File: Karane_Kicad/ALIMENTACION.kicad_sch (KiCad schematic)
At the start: 17 parts, among them J11 Conn_01x02_Socket, J9 Conn_01x02_Socket, SW4 SW_Push_SPDT, U24 CN3903

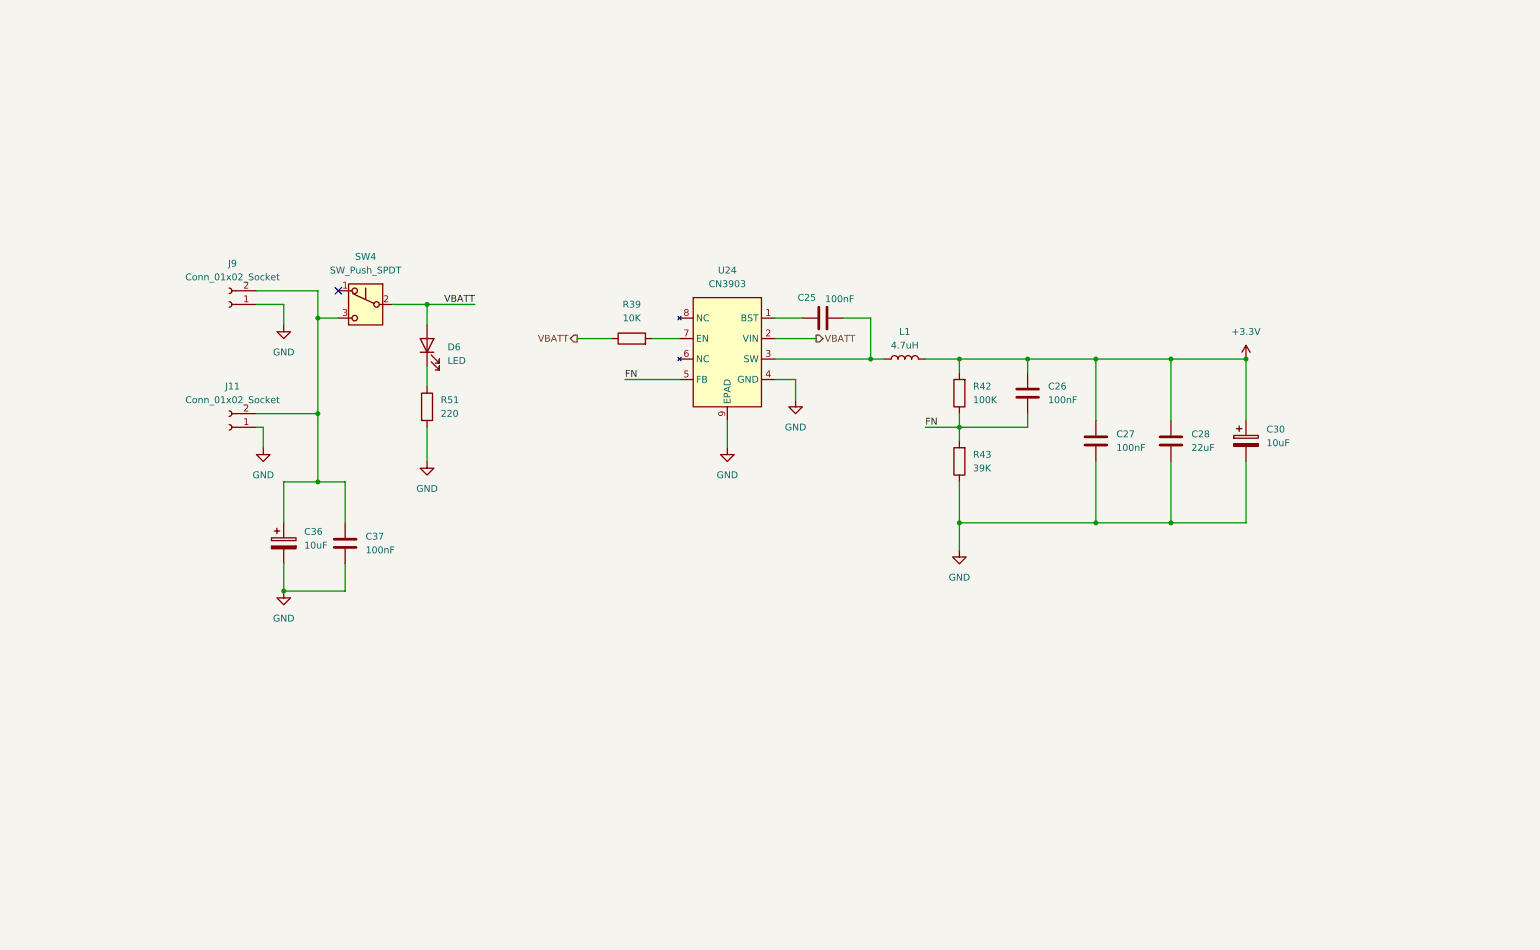
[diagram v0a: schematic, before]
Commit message: Agregado Mosfet dual
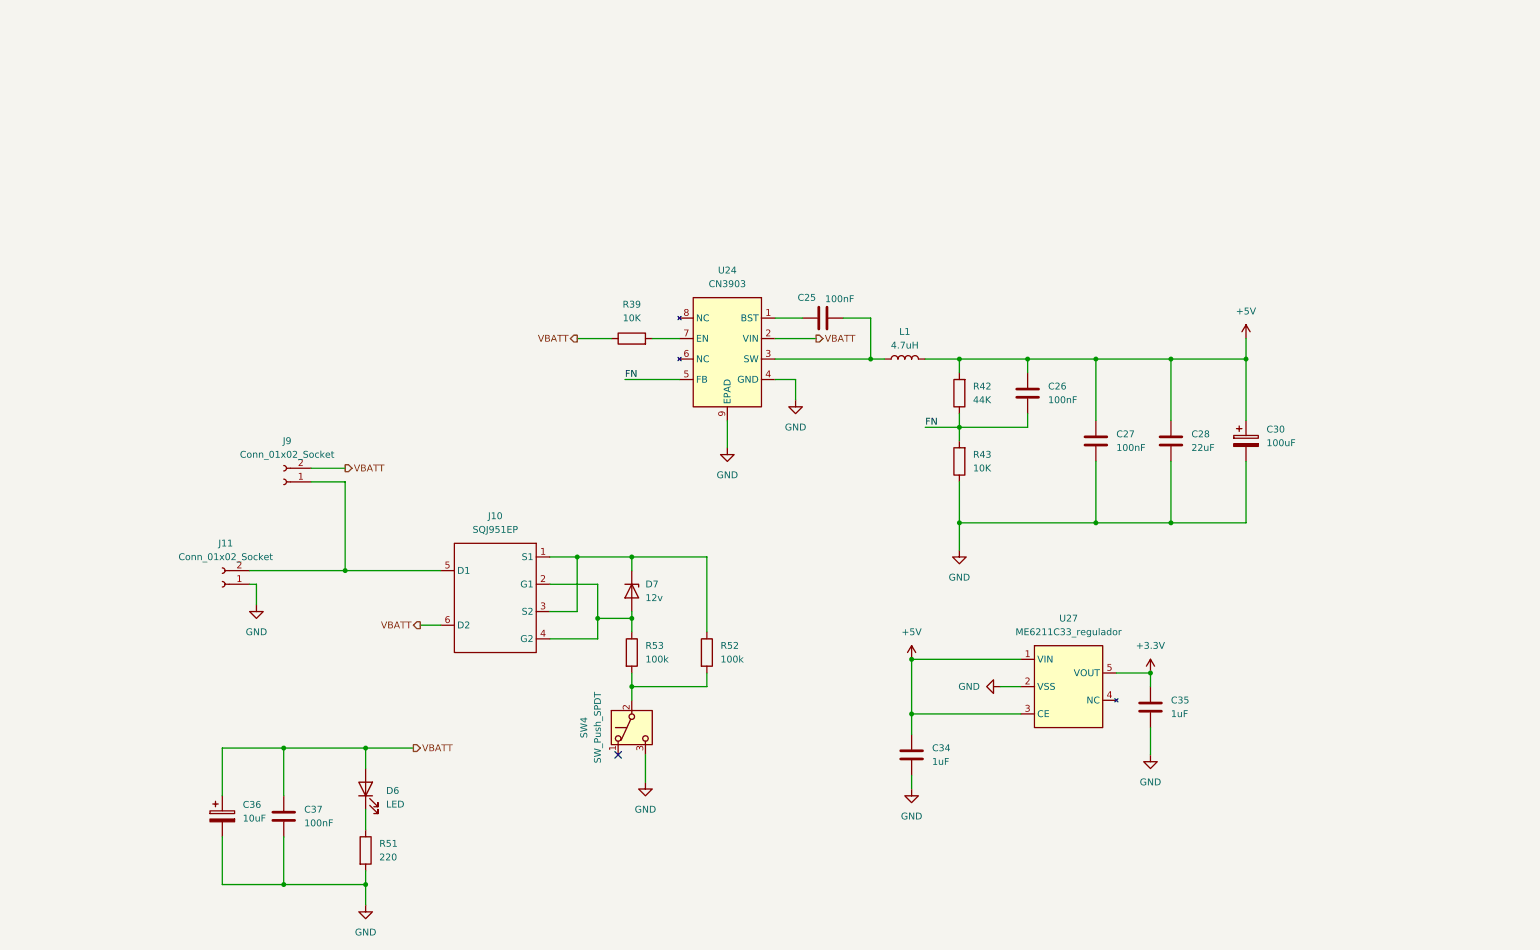
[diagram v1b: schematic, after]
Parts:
- added C34, C35: 1uF, Capacitor_SMD:C_0603_1608Metric_Pad1.08x0.95mm_HandSolder, symbol Device:C
- added D7: 12v, symbol Device:D_Zener
- added J10: SQJ951EP, Package_SO:PowerPAK_SO-8_Dual, symbol Micromouse_Library:SQJ951EP-T1_BE3
- added R52, R53: 100k, Resistor_SMD:R_0805_2012Metric_Pad1.20x1.40mm_HandSolder, symbol Device:R
- added U27: ME6211C33_regulador, Package_TO_SOT_SMD:SOT-23-5_HandSoldering, symbol Micromouse_Library:ME6211C33_regulador
- C30: value 10uF -> 100uF
- R42: value 100K -> 44K
- R43: value 39K -> 10K
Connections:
- net +3.3V: now also C35.1, U27.5 (VOUT); no longer C26.1, C27.1, C28.1, C30.1, L1.2, R42.2
- net GND: now also SW4.3 (C), C34.2, C35.2, U27.2 (VSS); no longer J9.1 (Pin_1)
- net VBATT: now also C36.1, C37.1, J9.2 (Pin_2), J10.6 (D2); no longer SW4.2 (B)
- new net: D7.1 (K), J10.1 (S1), J10.3 (S2), R52.1
- new net: D7.2 (A), J10.2 (G1), J10.4 (G2), R53.1
- new net: J10.5 (D1), J11.2 (Pin_2), J9.1 (Pin_1)
- new net: R52.2, R53.2, SW4.2 (B)
- new net +5V: C26.1, C27.1, C28.1, C30.1, C34.1, L1.2, R42.2, U27.1 (VIN), U27.3 (CE)
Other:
- moved on the sheet: C36, C37, D6, J11, J9, R51, SW4

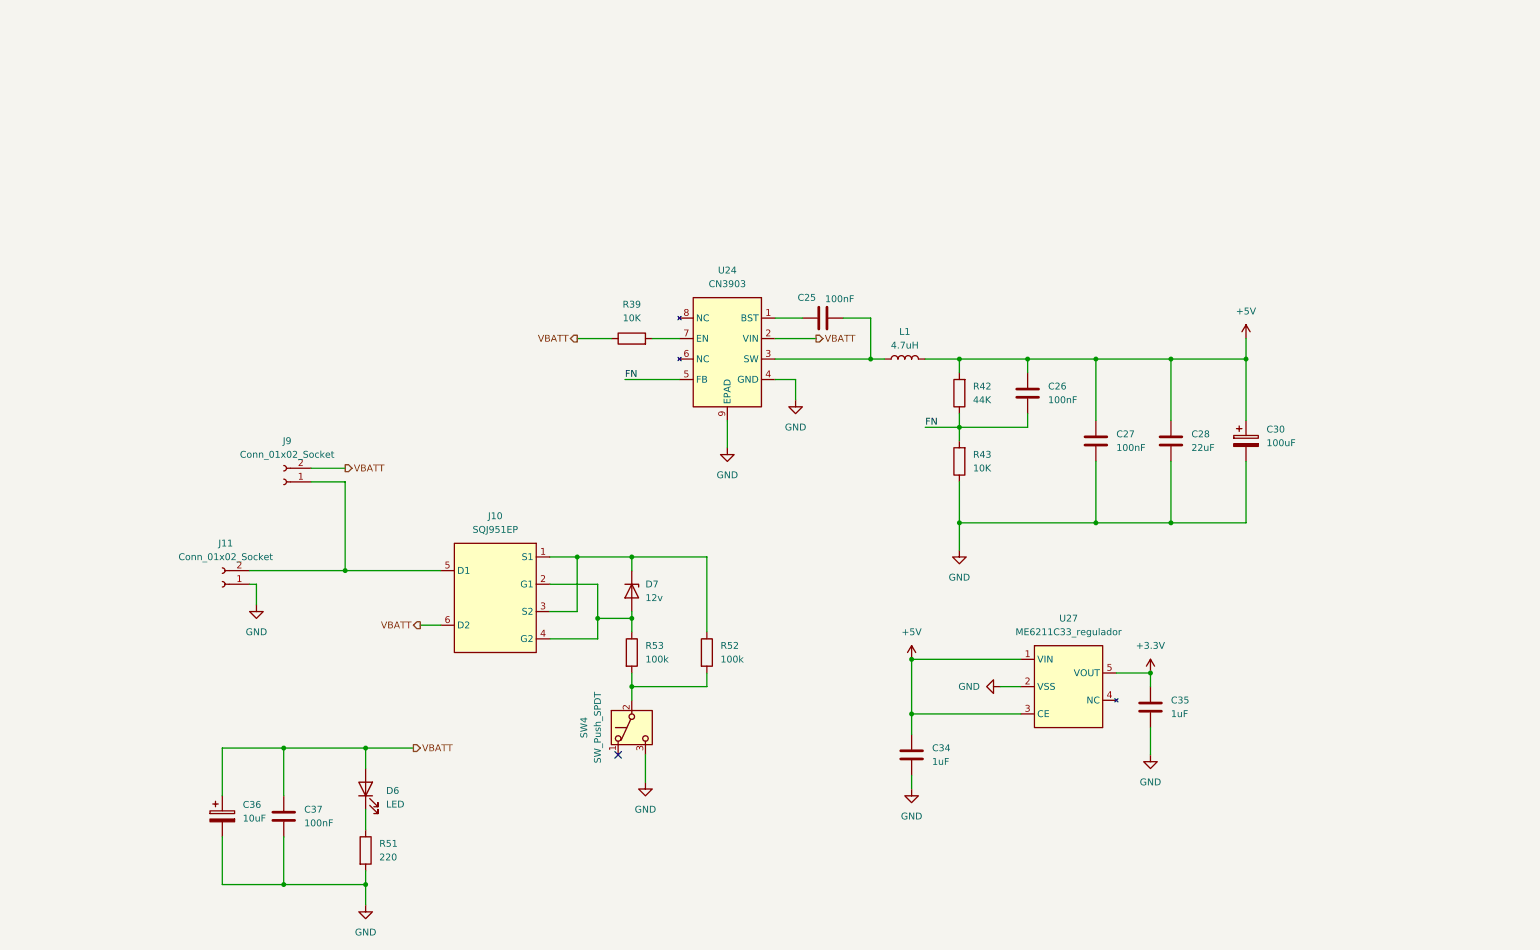
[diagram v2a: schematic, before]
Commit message: Agregado symbol de mosfet
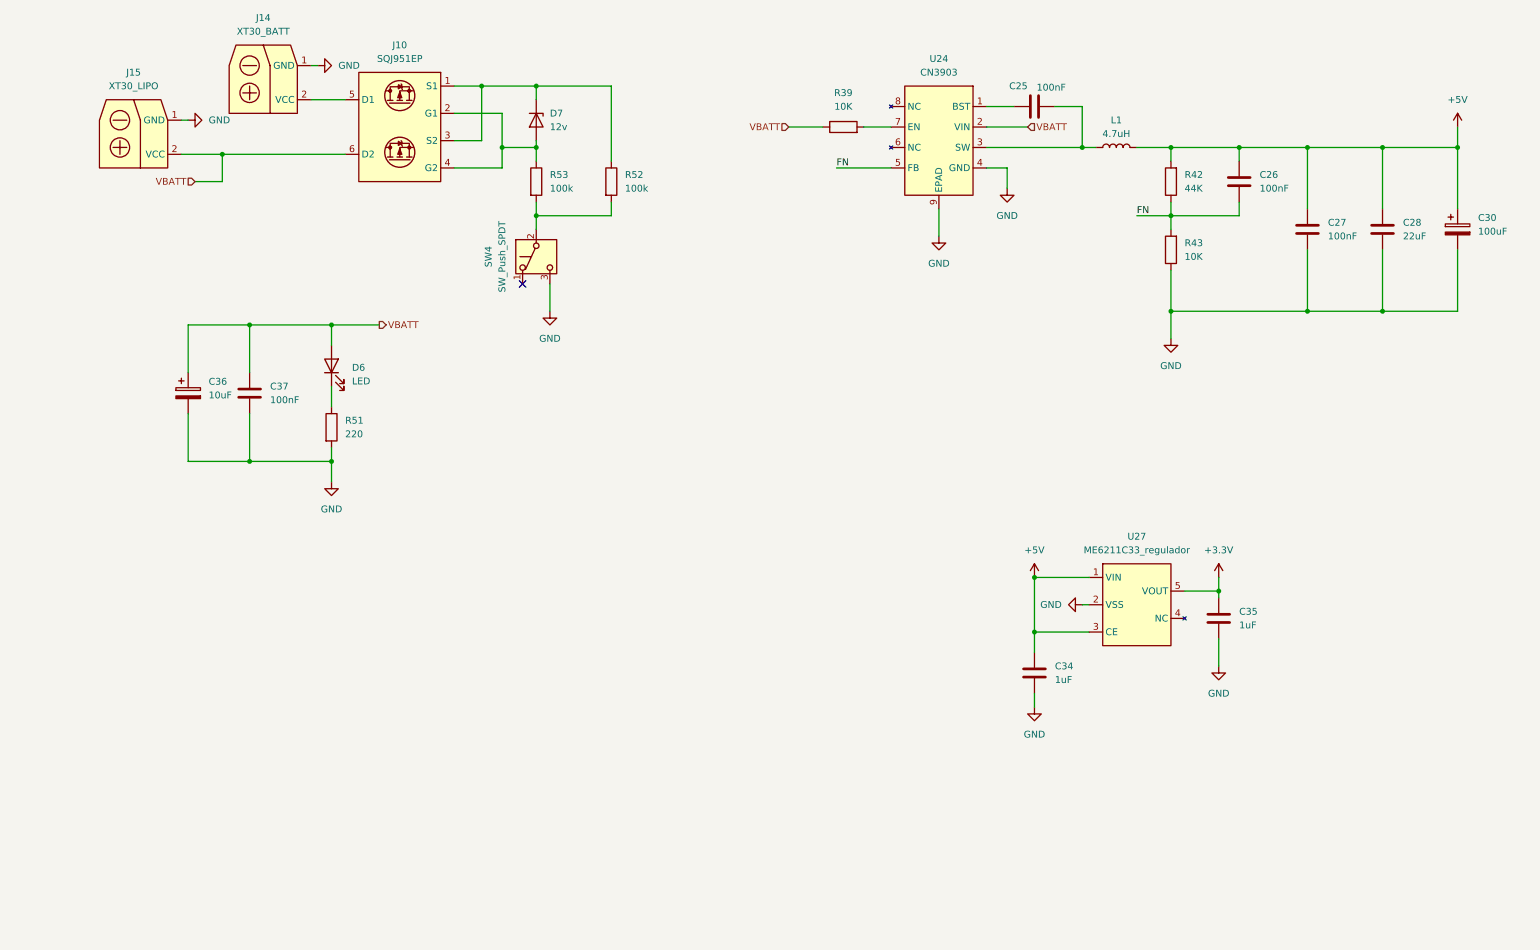
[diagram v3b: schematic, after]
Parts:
- removed J11, J9: Conn_01x02_Socket, Connector_Samtec_HPM_THT:Samtec_HPM-02-01-x-S_Straight_1x02_Pitch5.08mm, symbol Connector:Conn_01x02_Socket
- added J14: XT30_BATT, Connector_AMASS:AMASS_XT30U-F_1x02_P5.0mm_Vertical, symbol Micromouse_Library:Conector_XT30
- added J15: XT30_LIPO, Connector_AMASS:AMASS_XT30U-F_1x02_P5.0mm_Vertical, symbol Micromouse_Library:Conector_XT30
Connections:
- net GND: now also J14.1 (GND), J15.1 (GND)
- net VBATT: now also J15.2 (VCC)
- net at J10.5 (D1): now also J14.2 (VCC)
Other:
- moved on the sheet: C25, C26, C27, C28, C30, C34, C35, C36, C37, D6, D7, L1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

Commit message: Cambio de f103 a f401
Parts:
- removed D7: 12v, symbol Device:D_Zener
- removed J10: SQJ951EP, Package_SO:PowerPAK_SO-8_Dual, symbol Micromouse_Library:SQJ951EP-T1_BE3
- removed J15: XT30_LIPO, Connector_AMASS:AMASS_XT30U-F_1x02_P5.0mm_Vertical, symbol Micromouse_Library:Conector_XT30
- removed R52, R53: 100k, Resistor_SMD:R_0805_2012Metric_Pad1.20x1.40mm_HandSolder, symbol Device:R
- removed SW4: SW_Push_SPDT, Button_Switch_SMD:SW_SPDT_PCM12, symbol Switch:SW_Push_SPDT
- added D9: 12v, Diode_SMD:D_1206_3216Metric_Pad1.42x1.75mm_HandSolder, symbol Device:D_Zener
- added J11: XT30_BATT, Connector_AMASS:AMASS_XT30U-F_1x02_P5.0mm_Vertical, symbol Micromouse_Library:Conector_XT30
- added J12, J13: SQJ951EP, Package_SO:PowerPAK_SO-8_Dual, symbol Micromouse_Library:SQJ951EP-T1_BE3
- added R55, R57: 100k, Resistor_SMD:R_0805_2012Metric_Pad1.20x1.40mm_HandSolder, symbol Device:R
- added SW5: SW_Push_SPDT, Button_Switch_SMD:SW_SPDT_PCM12, symbol Switch:SW_Push_SPDT
- J14: value XT30_BATT -> XT30_LIPO
- renumbered C36 to C29, C37 to C30, C25 to C31, C34 to C32, C35 to C33, C26 to C34, C27 to C35, C28 to C36, C30 to C37, D6 to D10, R51 to R56, R39 to R58, R42 to R59, R43 to R60, U24 to U25, U27 to U26
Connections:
- net GND: now also J11.1 (GND), SW5.2 (B)
- net VBATT: now also J14.2 (VCC), J13.5 (D1), J13.6 (D2)
- new net: J11.2 (VCC), J12.5 (D1), J12.6 (D2)
- new net: D9.1 (K), J12.1 (S1), J12.3 (S2), J13.1 (S1), J13.3 (S2), R57.1
- new net: R55.2, R57.2, SW5.1 (A)
- new net: D9.2 (A), J12.2 (G1), J12.4 (G2), J13.2 (G1), J13.4 (G2), R55.1
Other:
- moved on the sheet: C29, C30, D10, R56

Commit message: planos de alimentacion hechos
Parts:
- added C42, C43: 1uF, Capacitor_SMD:C_0603_1608Metric_Pad1.08x0.95mm_HandSolder, symbol Device:C
- added U29: ME6211C33_regulador, Package_TO_SOT_SMD:SOT-23-5_HandSoldering, symbol Micromouse_Library:ME6211C33_regulador
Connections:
- net +5V: now also C42.1, U29.1 (VIN), U29.3 (CE)
- net GND: now also C42.2, C43.2, U29.2 (VSS)
- new net +3.3VA: C43.1, U29.5 (VOUT)

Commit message: finalizado pcb v2
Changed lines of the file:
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@@
 	)
 	(junction
-		(at 193.04 118.11)
-		(diameter 0)
-		(color 0 0 0 0)
-	)
-	(junction
 		(at 187.96 118.11)
 		(diameter 0)
@@
 	(wire
 		(pts
-			(xy 193.04 113.03) (xy 193.04 118.11)
-		)
-		(stroke
-			(width 0)
-			(type default)
-		)
-	)
-	(wire
-		(pts
 			(xy 237.49 129.54) (xy 247.65 129.54)
 		)
@@
 	(wire
 		(pts
-			(xy 193.04 118.11) (xy 187.96 118.11)
+			(xy 187.96 118.11) (xy 198.12 118.11)
 		)
 		(stroke
@@
 	(wire
 		(pts
-			(xy 198.12 118.11) (xy 193.04 118.11)
-		)
-		(stroke
-			(width 0)
-			(type default)
-		)
-	)
-	(wire
-		(pts
 			(xy 48.26 92.71) (xy 48.26 97.79)
 		)
@@
 	)
 	(symbol
+		(lib_id "power:PWR_FLAG")
+		(at 222.25 120.65 270)
+		(unit 1)
+		(body_style 1)
+		(exclude_from_sim no)
+		(in_bom yes)
+		(on_board yes)
+		(in_pos_files yes)
+		(dnp no)
+		(fields_autoplaced yes)
+		(property "Reference" "#FLG05"
+			(at 224.155 120.65 0)
+			(hide yes)
+			(show_name no)
+			(do_not_autoplace no)
+			(effects
+				(font
+					(size 1.27 1.27)
+				)
+			)
+		)
+		(property "Value" "PWR_FLAG"
+			(at 226.06 120.6499 90)
+			(show_name no)
+			(do_not_autoplace no)
+			(effects
+				(font
+					(size 1.27 1.27)
+				)
+				(justify left)
+			)
+		)
+		(property "Footprint" ""
+			(at 222.25 120.65 0)
+			(hide yes)
+			(show_name no)
+			(do_not_autoplace no)
+			(effects
+				(font
+					(size 1.27 1.27)
+				)
+			)
+		)
+		(property "Datasheet" ""
+			(at 222.25 120.65 0)
+			(hide yes)
+			(show_name no)
+			(do_not_autoplace no)
+			(effects
+				(font
+					(size 1.27 1.27)
+				)
+			)
+		)
+		(property "Description" "Special symbol for telling ERC where power comes from"
+			(at 222.25 120.65 0)
+			(hide yes)
+			(show_name no)
+			(do_not_autoplace no)
+			(effects
+				(font
+					(size 1.27 1.27)
+				)
+			)
+		)
+		(pin "1"
+		)
+		(instances
+			(project "Karane_Kicad"
+				(path "/65dfbecc-0fbf-480c-951c-b0d4a210bc14/e468b3be-adc2-4f31-828e-24b4692370ed"
+					(reference "#FLG05")
+					(unit 1)
+				)
+			)
+		)
+	)
+	(symbol
 		(lib_id "power:GND")
 		(at 213.36 73.66 0)
@@
 					(unit 1)
 				)
-			)
-		)
-	)
-	(symbol
-		(lib_id "power:PWR_FLAG")
-		(at 193.04 113.03 0)
-		(unit 1)
-		(body_style 1)
-		(exclude_from_sim no)
-		(in_bom yes)
-		(on_board yes)
-		(in_pos_files yes)
-		(dnp no)
-		(fields_autoplaced yes)
-		(property "Reference" "#FLG05"
-			(at 193.04 111.125 0)
-			(hide yes)
-			(show_name no)
-			(do_not_autoplace no)
-			(effects
-				(font
-					(size 1.27 1.27)
-				)
-			)
-		)
-		(property "Value" "PWR_FLAG"
-			(at 193.04 107.95 0)
-			(show_name no)
-			(do_not_autoplace no)
-			(effects
-				(font
-					(size 1.27 1.27)
-				)
-			)
-		)
-		(property "Footprint" ""
-			(at 193.04 113.03 0)
-			(hide yes)
-			(show_name no)
-			(do_not_autoplace no)
-			(effects
-				(font
-					(size 1.27 1.27)
-				)
-			)
-		)
-		(property "Datasheet" ""
-			(at 193.04 113.03 0)
-			(hide yes)
-			(show_name no)
-			(do_not_autoplace no)
-			(effects
-				(font
-					(size 1.27 1.27)
-				)
-			)
-		)
-		(property "Description" "Special symbol for telling ERC where power comes from"
-			(at 193.04 113.03 0)
-			(hide yes)
-			(show_name no)
-			(do_not_autoplace no)
-			(effects
-				(font
-					(size 1.27 1.27)
-				)
-			)
-		)
-		(pin "1"
-		)
-		(instances
-			(project "Karane_Kicad"
-				(path "/65dfbecc-0fbf-480c-951c-b0d4a210bc14/e468b3be-adc2-4f31-828e-24b4692370ed"
-					(reference "#FLG05")
-					(unit 1)
-				)

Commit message: Agregado agujeros a pcb
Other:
- moved on the sheet: C29, C30, D10, D9, J11, J12, J13, J14, R55, R56, R57, SW5
